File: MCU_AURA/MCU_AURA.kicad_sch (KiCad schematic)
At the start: 0 parts

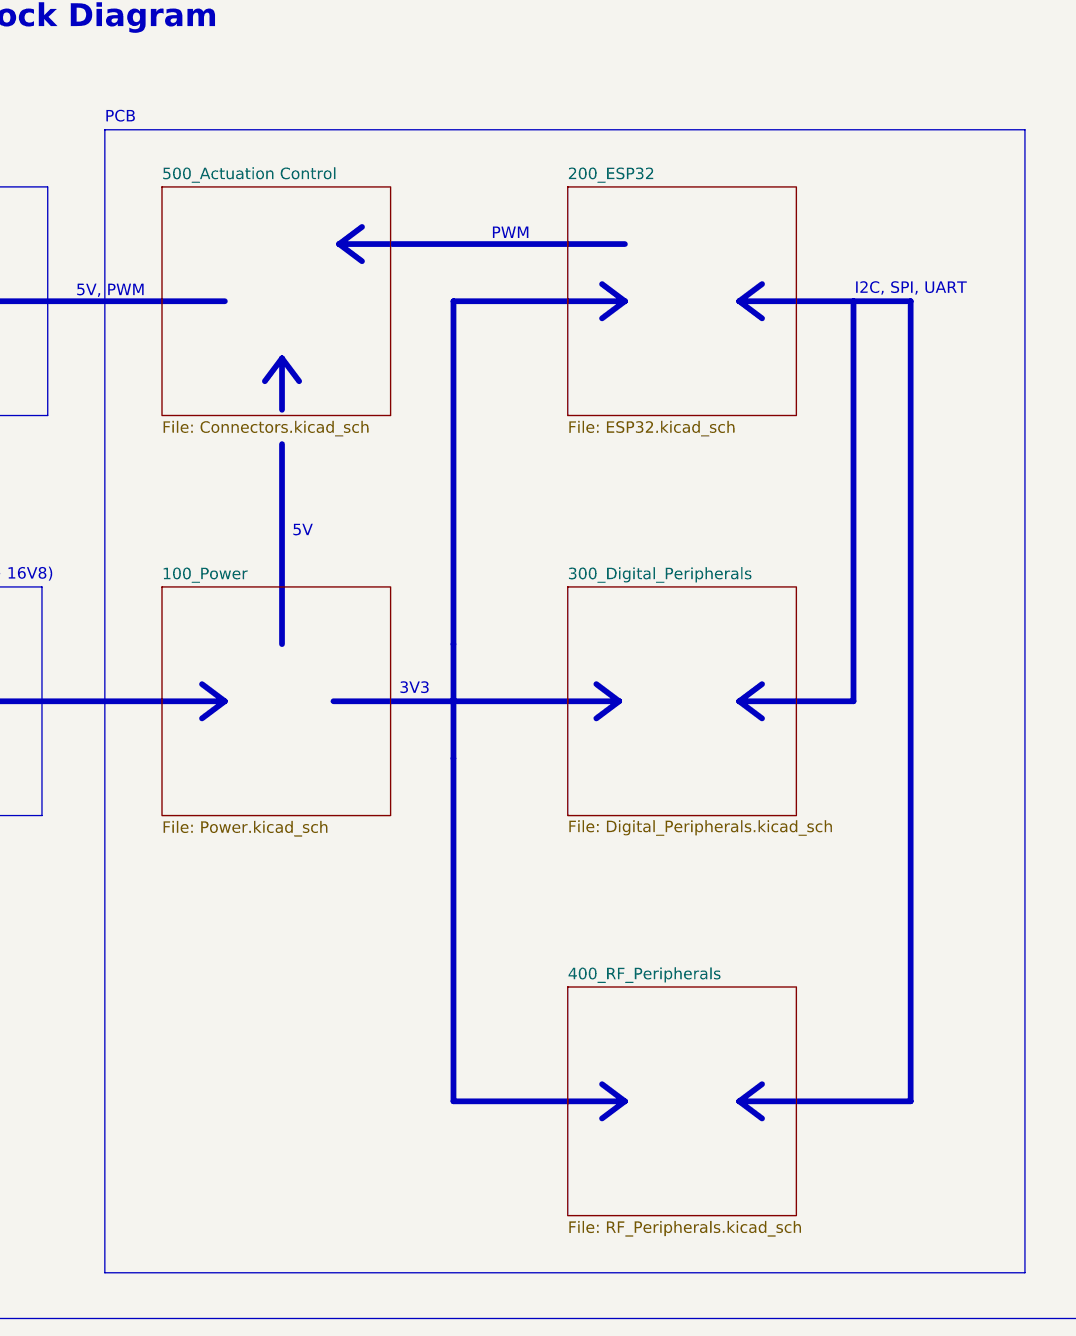
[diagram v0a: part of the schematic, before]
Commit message: Started Editing
Problem syncing desktop to laptop (libraries).
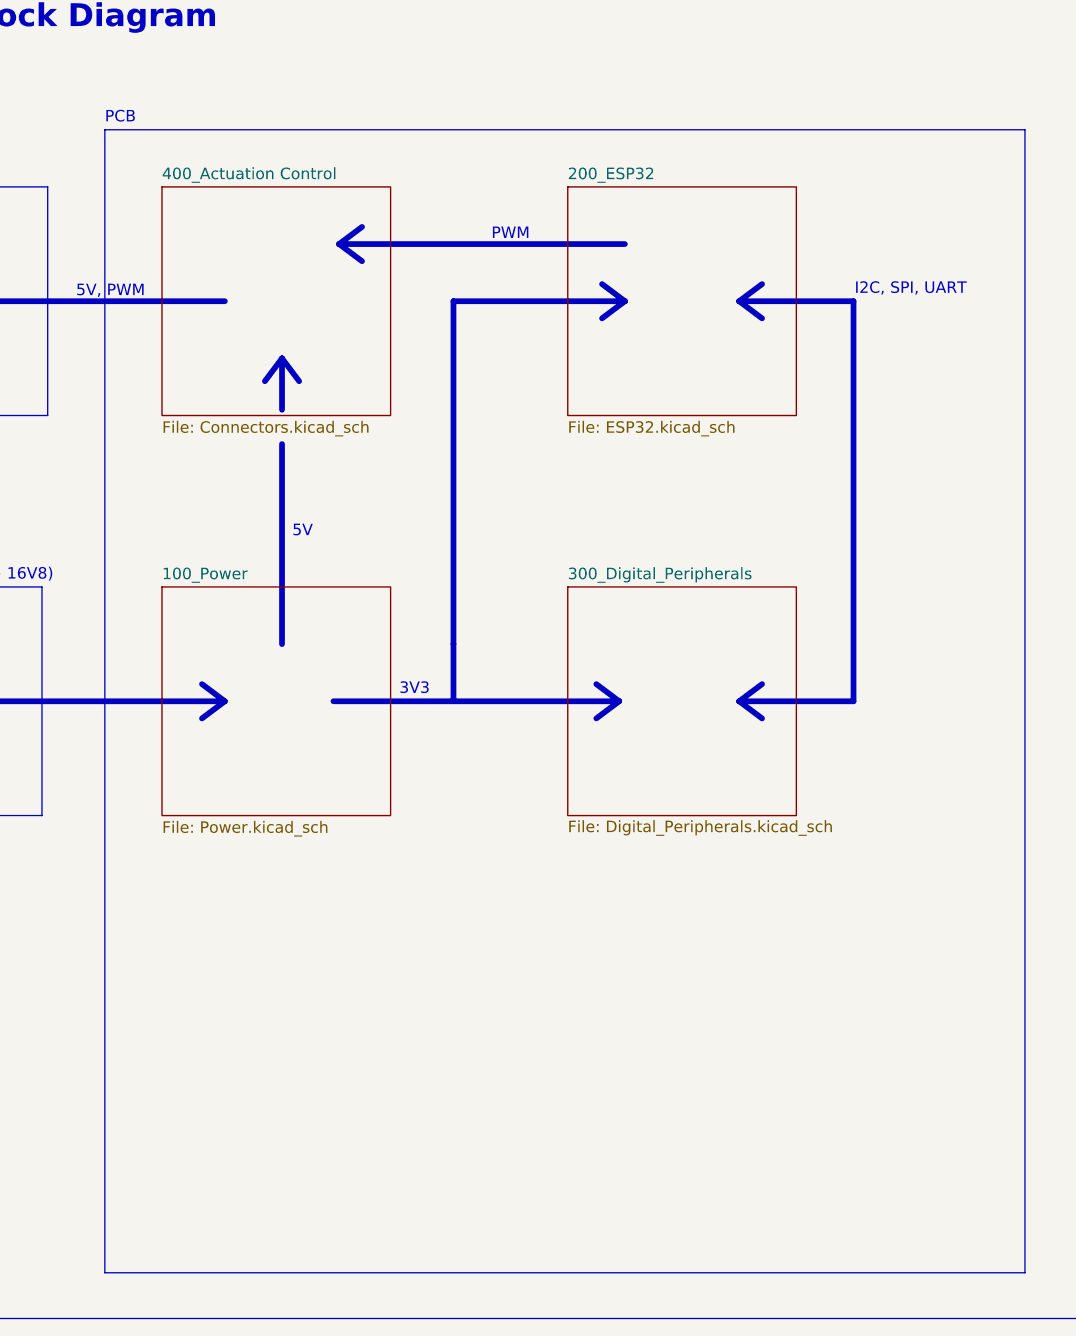
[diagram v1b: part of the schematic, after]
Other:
- sheet 500_Actuation Control renamed 400_Actuation Control
- removed sheet 400_RF_Peripherals
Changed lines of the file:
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@@
-	(polyline
-		(pts
-			(xy 129.54 152.4) (xy 132.08 150.495)
-		)
-		(stroke
-			(width 0.635)
-			(type solid)
-			(color 200 0 0 1)
-		)
-	)
 	(polyline
 		(pts
@@
 	(polyline
 		(pts
-			(xy 97.79 114.3) (xy 97.79 152.4)
-		)
-		(stroke
-			(width 0.635)
-			(type solid)
-		)
-	)
-	(polyline
-		(pts
 			(xy 78.74 69.85) (xy 76.835 72.39)
 		)
@@
 	(polyline
 		(pts
-			(xy 148.59 63.5) (xy 148.59 152.4)
-		)
-		(stroke
-			(width 0.635)
-			(type solid)
-			(color 200 0 0 1)
-		)
-	)
-	(polyline
-		(pts
 			(xy 116.205 107.95) (xy 113.665 109.855)
 		)
@@
 	(polyline
 		(pts
-			(xy 116.84 152.4) (xy 114.3 150.495)
-		)
-		(stroke
-			(width 0.635)
-			(type solid)
-		)
-	)
-	(polyline
-		(pts
 			(xy 78.74 69.85) (xy 78.74 75.565)
 		)
@@
 	(polyline
 		(pts
-			(xy 116.84 152.4) (xy 114.3 154.305)
-		)
-		(stroke
-			(width 0.635)
-			(type solid)
-		)
-	)
-	(polyline
-		(pts
 			(xy 72.39 107.95) (xy 69.85 106.045)
 		)
@@
 	(polyline
 		(pts
-			(xy 97.79 107.95) (xy 97.79 114.3)
-		)
-		(stroke
-			(width 0.635)
-			(type solid)
-		)
-	)
-	(polyline
-		(pts
 			(xy 129.54 63.5) (xy 132.08 61.595)
 		)
@@
 	(polyline
 		(pts
-			(xy 129.54 152.4) (xy 148.59 152.4)
-		)
-		(stroke
-			(width 0.635)
-			(type solid)
-			(color 200 0 0 1)
-		)
-	)
-	(polyline
-		(pts
-			(xy 97.79 152.4) (xy 116.84 152.4)
-		)
-		(stroke
-			(width 0.635)
-			(type solid)
-		)
-	)
-	(polyline
-		(pts
 			(xy 84.455 107.95) (xy 116.205 107.95)
 		)
@@
 	(polyline
 		(pts
-			(xy 142.24 63.5) (xy 148.59 63.5)
-		)
-		(stroke
-			(width 0.635)
-			(type solid)
-			(color 200 0 0 1)
-		)
-	)
-	(polyline
-		(pts
 			(xy 129.54 107.95) (xy 142.24 107.95)
 		)
@@
 			(type solid)
 			(color 200 0 0 1)
-		)
-	)
-	(polyline
-		(pts
-			(xy 129.54 152.4) (xy 132.08 154.305)
-		)
-		(stroke
-			(width 0.635)
-			(type solid)
-			(color 200 0 0 1)
-		)
-	)
-	(sheet
-		(at 110.49 139.7)
-		(size 25.4 25.4)
-		(exclude_from_sim no)
-		(in_bom yes)
-		(on_board yes)
-		(dnp no)
-		(fields_autoplaced yes)
-		(stroke
-			(width 0.1524)
-			(type solid)
-		)
-		(fill
-			(color 0 0 0 0.0000)
-		)
-		(property "Sheetname" "400_RF_Peripherals"
-			(at 110.49 138.9884 0)
-			(effects
-				(font
-					(size 1.27 1.27)
-				)
-				(justify left bottom)
-			)
-		)
-		(property "Sheetfile" "RF_Peripherals.kicad_sch"
-			(at 110.49 165.6846 0)
-			(effects
-				(font
-					(size 1.27 1.27)
-				)
-				(justify left top)
-			)
-		)
-		(instances
-			(project "Summer2025"
-				(path "/c0b09de1-c640-438f-9ef5-dda14a6aac71"
-					(page "5")
-				)
-			)
 		)
 	)
@@
 		)
 		(instances
-			(project "Summer2025"
+			(project "MCU_AURA"
 				(path "/c0b09de1-c640-438f-9ef5-dda14a6aac71"
 					(page "4")
@@
 		)
 		(instances
-			(project "Summer2025"
+			(project "MCU_AURA"
 				(path "/c0b09de1-c640-438f-9ef5-dda14a6aac71"
 					(page "3")
@@
 			(color 0 0 0 0.0000)
 		)
-		(property "Sheetname" "500_Actuation Control"
+		(property "Sheetname" "400_Actuation Control"
 			(at 65.405 50.0884 0)
 			(effects
@@
 		)
 		(instances
-			(project "Summer2025"
+			(project "MCU_AURA"
 				(path "/c0b09de1-c640-438f-9ef5-dda14a6aac71"
 					(page "6")
@@
 		)
 		(instances
-			(project "Summer2025"
+			(project "MCU_AURA"
 				(path "/c0b09de1-c640-438f-9ef5-dda14a6aac71"
 					(page "2")

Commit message: Initial Schematic Draft
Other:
- note added: "Be able to power 12 servos plus all on board electronics. Have power switching between USB and Battery. Have long range radio for communication. Use GPS, barometer, magnetometer, gyroscope, and acceleromter to perform sensor fusion. Use JTAG for debugging embedded software. Be programmable through the ESP-IDF programming framework. Able to be used in a variety of robotic systems: quadrupeds, dron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"
- note added: "Fix block diagram (it is outdated)"
- note added: "ToDos:"
- note removed: "Be able to power 8 servos plus all on board electronics. Have power switching between USB and Battery. Have long range radio for communication. Use GPS, barometer, magnetometer, gyroscope, and acceleromter to perform sensor fusion. Use JTAG for debugging embedded software. Be programmable through the ESP-IDF programming framework. Able to be used in a variety of robotic systems e.g. a quadrupedal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"
- title: Project Outline -> MCU AURA
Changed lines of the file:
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@@
 	(paper "A4")
 	(title_block
-		(title "Project Outline")
+		(title "MCU AURA")
 		(date "25-05-2025")
 		(rev "0.0.1")
 	)
 	(rectangle
-		(start 190.5 76.2)
-		(end 266.7 125.73)
+		(start 190.5 101.6)
+		(end 266.7 151.13)
+		(stroke
+			(width 0)
+			(type default)
+		)
+		(fill
+			(type none)
+		)
+	)
+	(rectangle
+		(start 190.5 38.1)
+		(end 266.7 87.63)
 		(stroke
 			(width 0)
@@
 		)
 	)
-	(text "3V3"
-		(exclude_from_sim no)
-		(at 93.472 106.68 0)
-		(effects
-			(font
-				(size 1.27 1.27)
-			)
-		)
-	)
-	(text "I2C, SPI, UART"
-		(exclude_from_sim no)
-		(at 148.59 62.23 0)
-		(effects
-			(font
-				(size 1.27 1.27)
-			)
-		)
-	)
-	(text "Be able to power 8 servos plus all on board electronics.\n\nHave power switching between USB and Battery. \n\nHave long range radio for communication.\n\nUse GPS, barometer, magnetometer, gyroscope, and acceleromter\nto perform sensor fusion.\n\nUse JTAG for debugging embedded software.\n\nBe programmable through the ESP-IDF programming framework.\n\nAble to be used in a variety of robotic systems e.g. a \nquadrupedal robot.\n\n"
-		(exclude_from_sim no)
-		(at 198.12 88.9 0)
-		(effects
-			(font
-				(size 1.27 1.27)
-				(thickness 0.1588)
-			)
-			(justify left top)
-		)
-	)
-	(text "PCB"
-		(exclude_from_sim no)
-		(at 59.055 43.18 0)
-		(effects
-			(font
-				(size 1.27 1.27)
-			)
-			(justify left)
-		)
-	)
-	(text "5V, PWM"
-		(exclude_from_sim no)
-		(at 59.69 62.484 0)
-		(effects
-			(font
-				(size 1.27 1.27)
-			)
-		)
-	)
-	(text "PWM"
-		(exclude_from_sim no)
-		(at 104.14 56.134 0)
-		(effects
-			(font
-				(size 1.27 1.27)
-			)
-		)
-	)
-	(text "Project Block Diagram\n"
-		(exclude_from_sim no)
-		(at 27.94 32.004 0)
+	(text "ToDos:"
+		(exclude_from_sim no)
+		(at 198.12 110.744 0)
 		(effects
 			(font
@@
 		)
 	)
+	(text "3V3"
+		(exclude_from_sim no)
+		(at 93.472 106.68 0)
+		(effects
+			(font
+				(size 1.27 1.27)
+			)
+		)
+	)
+	(text "I2C, SPI, UART"
+		(exclude_from_sim no)
+		(at 148.59 62.23 0)
+		(effects
+			(font
+				(size 1.27 1.27)
+			)
+		)
+	)
+	(text "Be able to power 12 servos plus all on board electronics.\n\nHave power switching between USB and Battery. \n\nHave long range radio for communication.\n\nUse GPS, barometer, magnetometer, gyroscope, and acceleromter\nto perform sensor fusion.\n\nUse JTAG for debugging embedded software.\n\nBe programmable through the ESP-IDF programming framework.\n\nAble to be used in a variety of robotic systems: quadrupeds,\ndrones, rockets, and fixed wings.\n\n"
+		(exclude_from_sim no)
+		(at 198.12 50.8 0)
+		(effects
+			(font
+				(size 1.27 1.27)
+				(thickness 0.1588)
+			)
+			(justify left top)
+		)
+	)
+	(text "PCB"
+		(exclude_from_sim no)
+		(at 59.055 43.18 0)
+		(effects
+			(font
+				(size 1.27 1.27)
+			)
+			(justify left)
+		)
+	)
+	(text "5V, PWM"
+		(exclude_from_sim no)
+		(at 59.69 62.484 0)
+		(effects
+			(font
+				(size 1.27 1.27)
+			)
+		)
+	)
+	(text "PWM"
+		(exclude_from_sim no)
+		(at 104.14 56.134 0)
+		(effects
+			(font
+				(size 1.27 1.27)
+			)
+		)
+	)
+	(text "Fix block diagram (it is outdated)"
+		(exclude_from_sim no)
+		(at 198.12 114.3 0)
+		(effects
+			(font
+				(size 1.27 1.27)
+				(thickness 0.1588)
+			)
+			(justify left top)
+		)
+	)
+	(text "Project Block Diagram\n"
+		(exclude_from_sim no)
+		(at 27.94 32.004 0)
+		(effects
+			(font
+				(size 2.54 2.54)
+				(thickness 0.508)
+				(bold yes)
+			)
+			(justify left)
+		)
+	)
 	(text "5V"
 		(exclude_from_sim no)
@@
 	(text "Project Goals:\n"
 		(exclude_from_sim no)
-		(at 198.12 85.09 0)
+		(at 198.12 46.99 0)
 		(effects
 			(font
@@
 			(project "MCU_AURA"
 				(path "/c0b09de1-c640-438f-9ef5-dda14a6aac71"
-					(page "6")
-				)
-			)
+					(page "5")
+				)
+			)

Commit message: Started Routing
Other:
- note added: "Fix block diagram (it is outdated) Change 4u7 to 0402 and 22u to 0805 Mark components as DNP for manufacturing"
- note removed: "Fix block diagram (it is outdated)"
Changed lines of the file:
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@@
 		)
 	)
-	(text "Fix block diagram (it is outdated)"
+	(text "Fix block diagram (it is outdated)\nChange 4u7 to 0402 and 22u to 0805\nMark components as DNP for manufacturing"
 		(exclude_from_sim no)
 		(at 198.12 114.3 0)

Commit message: First fully routed version
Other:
- note added: "5V/VBAT"
- note added: "AUX"
- note added: "GPS"
- note added: "I2C/Pyro"
- note added: "MCU"
- note added: "PDB"
- note added: "RADIO"
- note added: "RC RX"
- note added: "SBUS/IBUS"
- note added: "SERVOS / ESCS"
- note added: "SPI"
- note added: "SPI/I2C/ UART"
- note added: "UART"
- note added: "VBAT"
- note removed: "3V3"
- note removed: "5V, PWM"
- note removed: "I2C, SPI, UART"
- note removed: "PCB"
- note removed: "Servo Motors"
- note removed: "USB or Battery (7V2 -> 16V8)"

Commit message: Second Iteration MCU
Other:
- note removed: "Fix block diagram (it is outdated) Change 4u7 to 0402 and 22u to 0805 Mark components as DNP for manufacturing"
- note removed: "ToDos:"
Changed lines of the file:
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@@
-	)
-	(rectangle
-		(start 190.5 101.6)
-		(end 266.7 151.13)
-		(stroke
-			(width 0)
-			(type default)
-		)
-		(fill
-			(type none)
-		)
 	)
 	(rectangle
@@
 	)
 	(rectangle
-		(start 190.5 38.1)
-		(end 266.7 87.63)
+		(start 190.5 63.5)
+		(end 266.7 113.03)
 		(stroke
 			(width 0)
@@
 		)
 	)
-	(text "ToDos:"
-		(exclude_from_sim no)
-		(at 198.12 110.744 0)
+	(text "GPS"
+		(exclude_from_sim no)
+		(at 91.44 38.1 0)
+		(effects
+			(font
+				(size 1.27 1.27)
+				(thickness 0.508)
+				(bold yes)
+			)
+		)
+	)
+	(text "SPI"
+		(exclude_from_sim no)
+		(at 118.11 52.07 0)
+		(effects
+			(font
+				(size 1.27 1.27)
+			)
+			(justify left)
+		)
+	)
+	(text "SPI/I2C/\nUART"
+		(exclude_from_sim no)
+		(at 142.24 99.06 0)
+		(effects
+			(font
+				(size 1.27 1.27)
+			)
+		)
+	)
+	(text "UART\n"
+		(exclude_from_sim no)
+		(at 92.71 52.07 0)
+		(effects
+			(font
+				(size 1.27 1.27)
+			)
+			(justify left)
+		)
+	)
+	(text "Be able to power 12 servos plus all on board electronics.\n\nHave power switching between USB and Battery. \n\nHave long range radio for communication.\n\nUse GPS, barometer, magnetometer, gyroscope, and acceleromter\nto perform sensor fusion.\n\nUse JTAG for debugging embedded software.\n\nBe programmable through the ESP-IDF programming framework.\n\nAble to be used in a variety of robotic systems: quadrupeds,\ndrones, rockets, and fixed wings.\n\n"
+		(exclude_from_sim no)
+		(at 198.12 76.2 0)
+		(effects
+			(font
+				(size 1.27 1.27)
+				(thickness 0.1588)
+			)
+			(justify left top)
+		)
+	)
+	(text "SBUS/IBUS"
+		(exclude_from_sim no)
+		(at 136.652 74.93 0)
+		(effects
+			(font
+				(size 1.27 1.27)
+			)
+			(justify left)
+		)
+	)
+	(text "RADIO"
+		(exclude_from_sim no)
+		(at 116.84 38.1 0)
+		(effects
+			(font
+				(size 1.27 1.27)
+				(thickness 0.508)
+				(bold yes)
+			)
+		)
+	)
+	(text "PDB"
+		(exclude_from_sim no)
+		(at 46.99 88.9 0)
+		(effects
+			(font
+				(size 1.27 1.27)
+				(thickness 0.508)
+				(bold yes)
+			)
+		)
+	)
+	(text "I2C/Pyro"
+		(exclude_from_sim no)
+		(at 59.69 62.23 0)
+		(effects
+			(font
+				(size 1.27 1.27)
+			)
+			(justify left)
+		)
+	)
+	(text "Project Block Diagram\n"
+		(exclude_from_sim no)
+		(at 24.13 25.654 0)
 		(effects
 			(font
@@
 		)
 	)
-	(text "GPS"
-		(exclude_from_sim no)
-		(at 91.44 38.1 0)
-		(effects
-			(font
-				(size 1.27 1.27)
-				(thickness 0.508)
-				(bold yes)
-			)
-		)
-	)
-	(text "SPI"
-		(exclude_from_sim no)
-		(at 118.11 52.07 0)
-		(effects
-			(font
-				(size 1.27 1.27)
-			)
-			(justify left)
-		)
-	)
-	(text "SPI/I2C/\nUART"
-		(exclude_from_sim no)
-		(at 142.24 99.06 0)
-		(effects
-			(font
-				(size 1.27 1.27)
-			)
-		)
-	)
-	(text "UART\n"
-		(exclude_from_sim no)
-		(at 92.71 52.07 0)
-		(effects
-			(font
-				(size 1.27 1.27)
-			)
-			(justify left)
-		)
-	)
-	(text "Be able to power 12 servos plus all on board electronics.\n\nHave power switching between USB and Battery. \n\nHave long range radio for communication.\n\nUse GPS, barometer, magnetometer, gyroscope, and acceleromter\nto perform sensor fusion.\n\nUse JTAG for debugging embedded software.\n\nBe programmable through the ESP-IDF programming framework.\n\nAble to be used in a variety of robotic systems: quadrupeds,\ndrones, rockets, and fixed wings.\n\n"
-		(exclude_from_sim no)
-		(at 198.12 50.8 0)
-		(effects
-			(font
-				(size 1.27 1.27)
-				(thickness 0.1588)
-			)
-			(justify left top)
-		)
-	)
-	(text "SBUS/IBUS"
-		(exclude_from_sim no)
-		(at 136.652 74.93 0)
-		(effects
-			(font
-				(size 1.27 1.27)
-			)
-			(justify left)
-		)
-	)
-	(text "RADIO"
-		(exclude_from_sim no)
-		(at 116.84 38.1 0)
-		(effects
-			(font
-				(size 1.27 1.27)
-				(thickness 0.508)
-				(bold yes)
-			)
-		)
-	)
-	(text "PDB"
-		(exclude_from_sim no)
-		(at 46.99 88.9 0)
-		(effects
-			(font
-				(size 1.27 1.27)
-				(thickness 0.508)
-				(bold yes)
-			)
-		)
-	)
-	(text "I2C/Pyro"
-		(exclude_from_sim no)
-		(at 59.69 62.23 0)
-		(effects
-			(font
-				(size 1.27 1.27)
-			)
-			(justify left)
-		)
-	)
-	(text "Fix block diagram (it is outdated)\nChange 4u7 to 0402 and 22u to 0805\nMark components as DNP for manufacturing"
-		(exclude_from_sim no)
-		(at 198.12 114.3 0)
-		(effects
-			(font
-				(size 1.27 1.27)
-				(thickness 0.1588)
-			)
-			(justify left top)
-		)
-	)
-	(text "Project Block Diagram\n"
-		(exclude_from_sim no)
-		(at 24.13 25.654 0)
-		(effects
-			(font
-				(size 2.54 2.54)
-				(thickness 0.508)
-				(bold yes)
-			)
-			(justify left)
-		)
-	)
 	(text "MCU"
 		(exclude_from_sim no)
@@
 	(text "Project Goals:\n"
 		(exclude_from_sim no)
-		(at 198.12 46.99 0)
-		(effects
-			(font
+		(at 198.12 72.39 0)
+		(effects
+			(font
